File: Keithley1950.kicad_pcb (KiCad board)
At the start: 2 copper layers, 0 parts

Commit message: Initial placement on pcb
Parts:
- added C1: 47uF, Capacitor_SMD:CP_Elec_6.3x5.9, F.Cu at (78.0, 52.0)
- added C10: 1uF, Capacitor_SMD:C_0805_2012Metric, F.Cu at (60.2, 98.5)
- added C11: .1uF, Capacitor_SMD:C_0603_1608Metric, B.Cu at (72.8, 58.8)
- added C12: 3.3uF, Capacitor_SMD:C_0603_1608Metric, F.Cu at (66.8, 103.0)
- added C13: .1uF, Capacitor_SMD:C_0603_1608Metric, F.Cu at (70.2, 103.0)
- added C14: .1uF, Capacitor_SMD:C_0603_1608Metric, F.Cu at (40.8, 51.2)
- added C15: .1uF, Capacitor_SMD:C_0603_1608Metric, B.Cu at (53.6, 44.8)
- added C16: .1uF, Capacitor_SMD:C_0603_1608Metric, F.Cu at (67.8, 77.8)
- added C17: .1uF, Capacitor_SMD:C_0603_1608Metric, B.Cu at (59.2, 37.2)
- added C18: .1uF, Capacitor_SMD:C_0603_1608Metric, F.Cu at (60.2, 74.2)
- added C19: 610pF, Capacitor_SMD:C_0805_2012Metric, F.Cu at (55.0, 64.2)
- added C2: 47uF, Capacitor_SMD:CP_Elec_6.3x5.9, F.Cu at (69.5, 52.0)
- added C20: 110pF, Capacitor_SMD:C_0805_2012Metric, F.Cu at (55.0, 73.2)
- added C21: 5pF, project:MURATA_TZ03, F.Cu at (68.5, 84.0)
- added C22: 47pF, Capacitor_SMD:C_0805_2012Metric, F.Cu at (64.5, 63.5)
- added C23: 0.1uF, Capacitor_THT:C_Rect_L18.0mm_W5.0mm_P15.00mm_FKS3_FKP3, F.Cu at (55.5, 92.0)
- added C24: 5pF, project:MURATA_TZ03, F.Cu at (57.0, 84.0)
- added C3: 47uF, Capacitor_SMD:CP_Elec_6.3x5.9, F.Cu at (61.0, 52.0)
- added C4: 470pF, Capacitor_SMD:C_0805_2012Metric, F.Cu at (83.0, 54.8)
- added C5: .1uF, Capacitor_SMD:C_0603_1608Metric, B.Cu at (69.5, 55.0)
- added C6: .1uF, Capacitor_SMD:C_0603_1608Metric, F.Cu at (74.5, 101.2)
- added C7: 10uF, Capacitor_SMD:CP_Elec_5x5.4, F.Cu at (75.8, 95.5)
- added C8: .1uF, Capacitor_SMD:C_0603_1608Metric, F.Cu at (69.2, 90.5)
- added C9: 10uF, Capacitor_SMD:C_0805_2012Metric, F.Cu at (62.8, 95.5)
- added D1: S3M, Diode_SMD:D_SMB-SMC_Universal_Handsoldering, B.Cu at (61.5, 32.0)
- added D2: S3M, Diode_SMD:D_SMB-SMC_Universal_Handsoldering, B.Cu at (73.5, 32.0)
- added D3: S3M, Diode_SMD:D_SMB-SMC_Universal_Handsoldering, B.Cu at (67.5, 39.0)
- added D4: S3M, Diode_SMD:D_SMB-SMC_Universal_Handsoldering, B.Cu at (61.5, 46.0)
- added D5: S3M, Diode_SMD:D_SMB-SMC_Universal_Handsoldering, B.Cu at (73.5, 46.0)
- added D6: S3M, Diode_SMD:D_SMB-SMC_Universal_Handsoldering, B.Cu at (63.0, 76.8)
- added D7: S3M, Diode_SMD:D_SMB-SMC_Universal_Handsoldering, B.Cu at (63.0, 69.8)
- added H1: MountingHole_Pad, MountingHole:MountingHole_3.2mm_M3_Pad_Via, F.Cu at (85.0, 105.0)
- added H2: MountingHole_Pad, MountingHole:MountingHole_3.2mm_M3_Pad_Via, F.Cu at (34.2, 58.5)
- added H3: MountingHole_Pad, MountingHole:MountingHole_3.2mm_M3_Pad_Via, F.Cu at (85.0, 25.0)
- added J1: Conn_01x14, Package_DIP:DIP-14_W7.62mm_Socket_LongPads, F.Cu at (80.0, 59.0)
- added J2: Conn_01x03, TerminalBlock_Phoenix:TerminalBlock_Phoenix_PT-1,5-3-5.0-H_1x03_P5.00mm_Horizontal, F.Cu at (84.0, 37.0)
- added J3: Conn_01x02, TerminalBlock_Phoenix:TerminalBlock_Phoenix_PT-1,5-2-5.0-H_1x02_P5.00mm_Horizontal, F.Cu at (84.0, 96.0)
- added K1: Relay_SP2P, Relay_THT:Relay_SPST_StandexMeder_SIL_Form1A, F.Cu at (48.2, 47.5)
- added K2: Relay_SP2P, Relay_THT:Relay_SPST_StandexMeder_SIL_Form1A, F.Cu at (48.2, 40.8)
- added K3: Relay_SP3P, Relay_THT:Relay_SPDT_SANYOU_SRD_Series_Form_C, F.Cu at (32.2, 28.8)
- added K4: Relay_SP2P, Relay_THT:Relay_SPST_StandexMeder_SIL_Form1A, F.Cu at (48.2, 65.5)
- added K5: Relay_SP2P, Relay_THT:Relay_SPST_StandexMeder_SIL_Form1A, F.Cu at (48.2, 72.2)
- added K6: Relay_SP3P, Relay_THT:Relay_SPDT_SANYOU_SRD_Series_Form_C, F.Cu at (32.2, 101.2)
- added K7: Relay_SP3P, Relay_THT:Relay_SPDT_SANYOU_SRD_Series_Form_C, F.Cu at (32.2, 84.2)
- added Q1: MMBFJ111, Package_TO_SOT_SMD:SOT-23, F.Cu at (54.5, 44.5)
- added Q2: MMBFJ111, Package_TO_SOT_SMD:SOT-23, F.Cu at (84.8, 50.8)
- added Q3: MMBFJ111, Package_TO_SOT_SMD:SOT-23, F.Cu at (54.5, 40.0)
- added Q4: MMBFJ111, Package_TO_SOT_SMD:SOT-23, F.Cu at (86.5, 78.0)
- added Q5: MMBT3906, Package_TO_SOT_SMD:SOT-23, F.Cu at (49.0, 59.0)
- added Q6: MMBT3906, Package_TO_SOT_SMD:SOT-23, F.Cu at (49.0, 55.0)
- added Q7: MMBFJ111, Package_TO_SOT_SMD:SOT-23, F.Cu at (64.5, 60.0)
- added Q8: MMBT3906, Package_TO_SOT_SMD:SOT-23, F.Cu at (68.5, 60.0)
- added R1: 10k, Resistor_SMD:R_0805_2012Metric, B.Cu at (76.0, 38.5)
- added R10: 4R7, Resistor_SMD:R_0805_2012Metric, F.Cu at (59.0, 36.5)
- added R11: 100k, Resistor_SMD:R_0805_2012Metric, F.Cu at (82.5, 78.0)
- added R12: 4R3, Resistor_SMD:R_0805_2012Metric, F.Cu at (63.5, 36.5)
- added R13: 5R1, Resistor_SMD:R_2512_6332Metric, B.Cu at (85.0, 52.5)
- added R14: R47, Resistor_SMD:R_2512_6332Metric, F.Cu at (66.5, 31.5)
- added R15: R43, Resistor_SMD:R_2512_6332Metric, F.Cu at (57.5, 31.5)
- added R16: 10k, Resistor_SMD:R_0805_2012Metric, F.Cu at (54.0, 59.8)
- added R17: 0R1, project:R_2512_With_10mm_axial, F.Cu at (62.0, 25.0)
- added R18: 10k, Resistor_SMD:R_0805_2012Metric, F.Cu at (54.0, 55.8)
- added R19: 10M, Resistor_SMD:R_0805_2012Metric, F.Cu at (62.8, 99.0)
- added R2: 10k, Resistor_SMD:R_0805_2012Metric, B.Cu at (78.5, 38.5)
- added R20: 2k, Resistor_SMD:R_0805_2012Metric, F.Cu at (55.0, 66.8)
- added R21: 27k, Resistor_SMD:R_0805_2012Metric, F.Cu at (66.0, 69.0)
- added R22: 10k, Resistor_SMD:R_0805_2012Metric, F.Cu at (55.0, 70.8)
- added R23: 24k, Resistor_SMD:R_0805_2012Metric, F.Cu at (64.5, 66.0)
- added R24: 3k, Resistor_SMD:R_0805_2012Metric, F.Cu at (62.0, 69.0)
- added R25: 1M, Resistor_SMD:R_0805_2012Metric, F.Cu at (62.5, 85.0)
- added R26: 1M, Resistor_SMD:R_0805_2012Metric, F.Cu at (58.0, 78.0)
- added R27: 10k, Resistor_SMD:R_0805_2012Metric, F.Cu at (87.0, 86.5)
- added R28: 100k, Resistor_SMD:R_0805_2012Metric, F.Cu at (68.5, 63.5)
- added R3: 470R, Resistor_SMD:R_0805_2012Metric, F.Cu at (59.0, 43.5)
- added R4: 100k, Resistor_SMD:R_0805_2012Metric, B.Cu at (51.5, 41.5)
- added R5: 430R, Resistor_SMD:R_0805_2012Metric, F.Cu at (63.5, 43.5)
- added R6: 47R, Resistor_SMD:R_0805_2012Metric, F.Cu at (63.5, 40.0)
- added R7: 100k, Resistor_SMD:R_0805_2012Metric, F.Cu at (85.8, 54.8)
- added R8: 100k, Resistor_SMD:R_0805_2012Metric, B.Cu at (51.5, 37.0)
- added R9: 43R, Resistor_SMD:R_0805_2012Metric, F.Cu at (59.0, 40.0)
- added TP1: TestPoint, TestPoint:TestPoint_Pad_D2.5mm, F.Cu at (58.2, 46.2)
- added TP2: TestPoint, TestPoint:TestPoint_Pad_D2.5mm, F.Cu at (82.5, 82.5)
- added TP3: TestPoint, TestPoint:TestPoint_Pad_D2.5mm, F.Cu at (63.0, 91.0)
- added TP4: TestPoint, TestPoint:TestPoint_Pad_D2.5mm, F.Cu at (61.0, 105.0)
- added TP5: TestPoint, TestPoint:TestPoint_Pad_D2.5mm, F.Cu at (69.5, 73.5)
- added U1: TL082, Package_SO:SOIC-8_3.9x4.9mm_P1.27mm, B.Cu at (55.5, 39.0)
- added U2: LM339, Package_SO:SOIC-14_3.9x8.7mm_P1.27mm, F.Cu at (71.2, 41.0)
- added U3: 74LS138, Package_SO:SOIC-16_3.9x9.9mm_P1.27mm, B.Cu at (63.0, 58.0)
- added U4: AD8436, Package_SO:QSOP-20_3.9x8.7mm_P0.635mm, F.Cu at (68.2, 97.0)
- added U5: ULN2003, Package_SO:SOIC-16_3.9x9.9mm_P1.27mm, F.Cu at (42.5, 57.2)
- added U6: 74HC4094, Package_SO:SOIC-16_3.9x9.9mm_P1.27mm, B.Cu at (74.5, 65.0)
- added U7: TL082, Package_SO:SOIC-8_3.9x4.9mm_P1.27mm, F.Cu at (64.0, 76.0)
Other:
- board outline added: 60 x 90 mm
- net class Default: trace_width 0.25 -> 0.3
- net class pwr added: clearance 0.3, trace_width 0.5, via_dia 1, via_drill 0.6
- rule pad_to_mask_clearance: 0.051 -> 0.02
- rule solder_mask_min_width: 0.25 -> 0.19
- rule trace_min: 0.2 -> 0.3

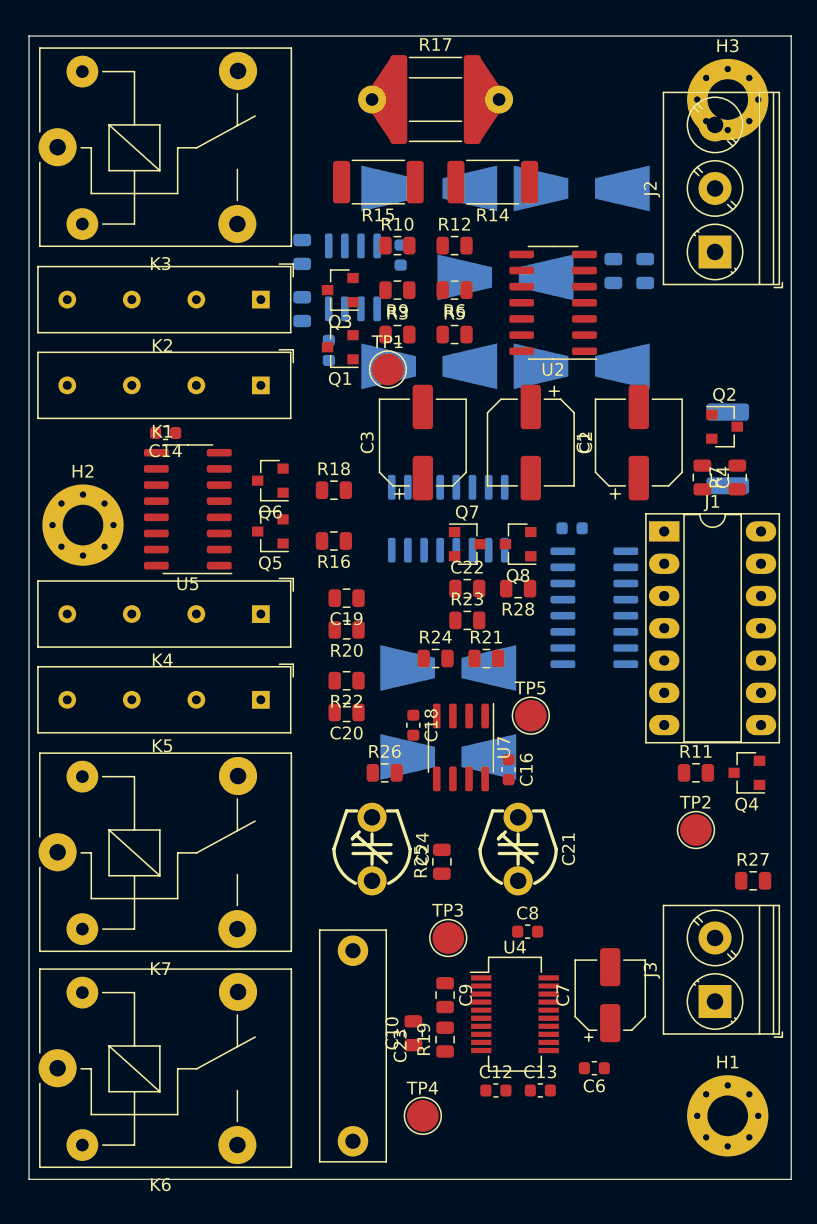
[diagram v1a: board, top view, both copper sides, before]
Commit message: Optimized placement
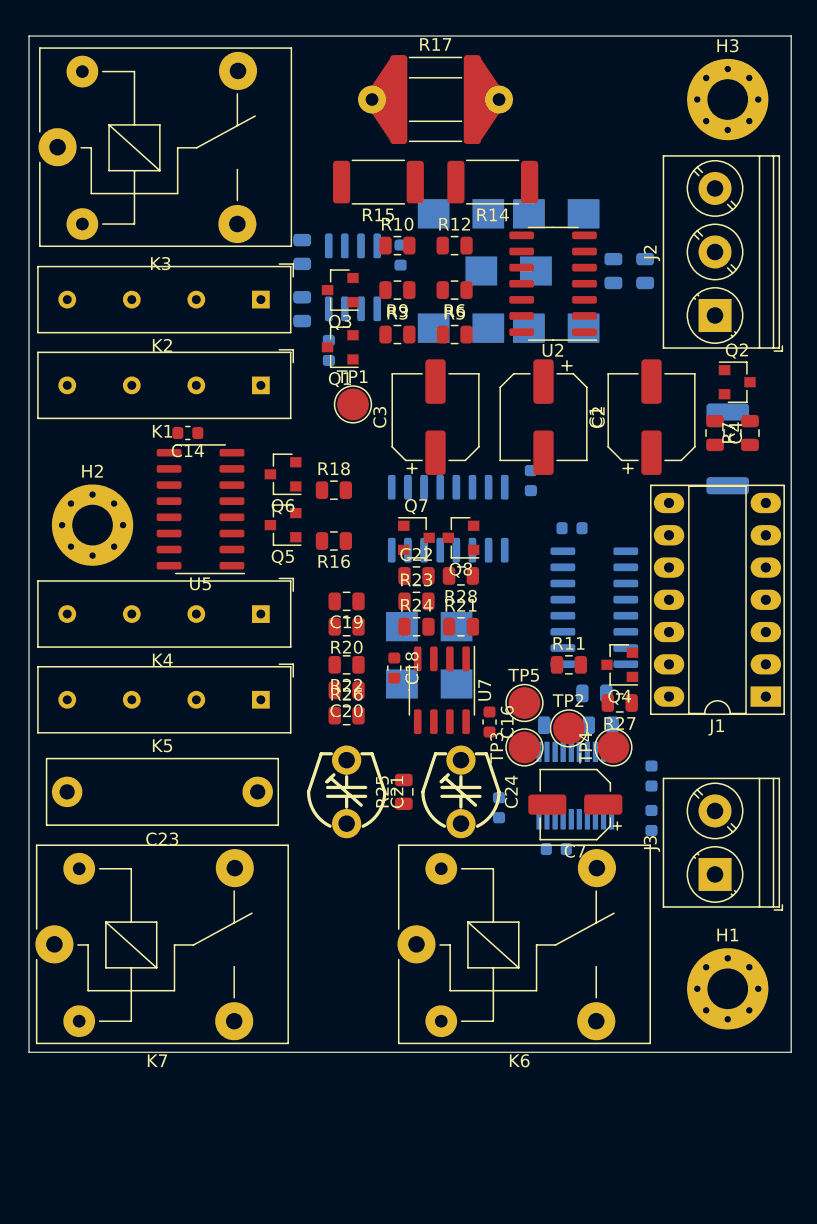
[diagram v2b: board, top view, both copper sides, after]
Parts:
- C10, C12, C13, C6, C8, C9, R19, U4: moved to B.Cu
- D1, D2, D3, D4, D5, D6, D7: footprint Diode_SMD:D_SMB-SMC_Universal_Handsoldering -> Diode_SMD:D_SMB
- moved TP4 32.6 mm to (76.0, 76.0), turned to 90 degrees
- moved C10 30.3 mm to (74.5, 71.8), turned to 180 degrees
- moved K6 29.9 mm to (60.5, 91.5)
- moved C12 27.6 mm to (79.0, 78.2), turned to 270 degrees
- moved R19 27.6 mm to (75.0, 74.2), turned to 180 degrees
- moved C13 23.0 mm to (79.0, 81.8), turned to 270 degrees
- moved C9 23.0 mm to (71.5, 74.2), turned to 0 degrees
- moved U4 18.6 mm to (73.0, 79.0), turned to 270 degrees
- moved C6 17.5 mm to (71.5, 84.0), turned to 0 degrees
- moved R27 17.5 mm to (76.5, 72.5), turned to 180 degrees
- moved TP3 16.2 mm to (69.0, 76.0), turned to 90 degrees
- moved J1 15.3 mm to (88.0, 72.0), turned to 180 degrees
- moved C7 15.2 mm to (73.0, 80.5), turned to 180 degrees
- moved C23 14.6 mm to (48.0, 79.5), turned to 180 degrees
- moved C21 14.2 mm to (55.0, 79.5)
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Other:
- board size 60 x 90 mm -> 60 x 80 mm

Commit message: More optimizations
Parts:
- C12: footprint Capacitor_SMD:C_0603_1608Metric -> Capacitor_SMD:C_0805_2012Metric
- R1, R2: moved to F.Cu
- moved C6 4.74 mm to (67.0, 82.5), turned to 270 degrees
- moved R2 3.30 mm to (77.0, 35.6), turned to 90 degrees
- moved D1 2.69 mm to (66.5, 33.0)
- moved D2 2.69 mm to (74.0, 33.0)
- moved D3 2.69 mm to (70.2, 37.5)
- moved D4 2.69 mm to (66.5, 42.0)
- moved D5 2.69 mm to (74.0, 42.0)
- moved C15 2.12 mm to (55.1, 46.2)
- moved C17 2.12 mm to (60.8, 38.8)
- moved R4 2.12 mm to (53.0, 43.0)
- moved R8 2.12 mm to (53.0, 38.5)
- moved U1 2.12 mm to (57.0, 40.5)
- moved R13 1.80 mm to (84.0, 51.0), turned to 180 degrees
- moved C8 1.75 mm to (67.0, 79.0)
- moved R1 1.41 mm to (77.0, 39.5)

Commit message: Manual routing done
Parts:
- R27: moved to B.Cu
- moved R27 14.2 mm to (74.0, 58.5)
- moved R16 6.54 mm to (54.8, 53.2)
- moved R28 6.50 mm to (64.0, 56.0), turned to 0 degrees
- moved Q5 5.80 mm to (50.8, 52.8)
- moved C11 2.50 mm to (70.2, 58.8)
- moved Q6 2.14 mm to (50.8, 56.5)
- moved C23 1.00 mm to (49.0, 79.5)
- moved H2 1.00 mm to (36.0, 58.5)
- moved K1 1.00 mm to (49.2, 47.5)
- moved K2 1.00 mm to (49.2, 40.8)
- moved K3 1.00 mm to (33.2, 28.8)
- moved K4 1.00 mm to (49.2, 65.5)
- moved K5 1.00 mm to (49.2, 72.2)
- moved K7 1.00 mm to (33.0, 91.5)
- moved R18 0.79 mm to (54.8, 55.5)
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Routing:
- net GNDA: track 0.00 -> 254.4 mm, vias 0 -> 19
- net +5V: track 0.00 -> 195.4 mm, vias 0 -> 2
- net -15V: track 0.00 -> 119.7 mm, vias 0 -> 2
- net /AMPS_INP: track 0.00 -> 112.5 mm
- net +15V: track 0.00 -> 106.4 mm, vias 0 -> 6
- net /SHUNT_SIGNAL: track 0.00 -> 98.4 mm, vias 0 -> 6
- net /INPUT_LO: track 0.00 -> 84.2 mm
- net Net-(C21-Pad2): track 0.00 -> 58.4 mm, vias 0 -> 1
- net Net-(K6-Pad5): track 0.00 -> 49.7 mm, vias 0 -> 1
- net Net-(K3-Pad5): track 0.00 -> 42.1 mm
- net /SHUNT_TRMS_SW: track 0.00 -> 41.7 mm, vias 0 -> 1
- net Net-(U3-Pad5): track 0.00 -> 39.3 mm, vias 0 -> 3
- net Net-(U5-Pad4): track 0.00 -> 34.8 mm, vias 0 -> 3
- net /SIGNAL_GUARD: track 0.00 -> 34.4 mm, vias 0 -> 1
- net Net-(U5-Pad3): track 0.00 -> 33.1 mm, vias 0 -> 3
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- added copper zone on B.Cu, net GNDA
- added copper zone on F.Cu, net GNDA
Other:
- net class pwr: clearance 0.3 -> 0.2

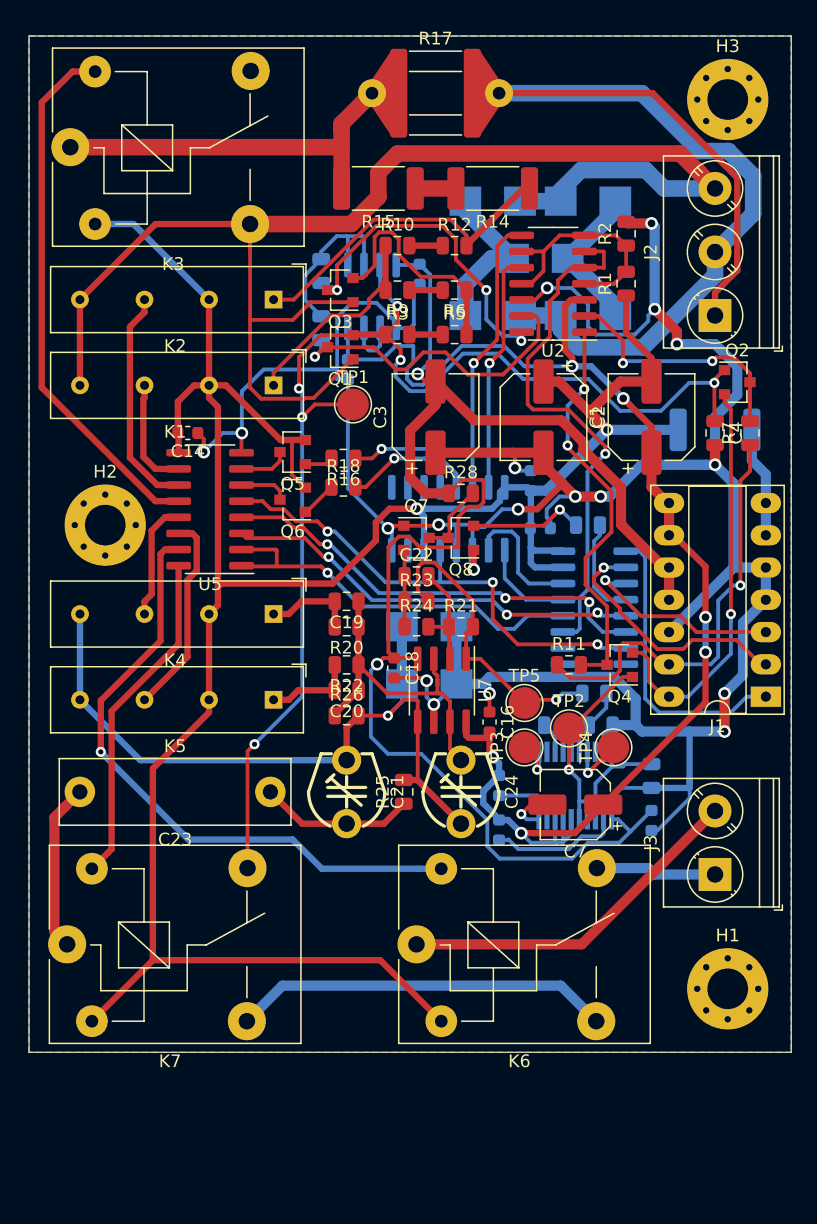
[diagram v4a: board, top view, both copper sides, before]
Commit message: Clean up silkscreen, add logos
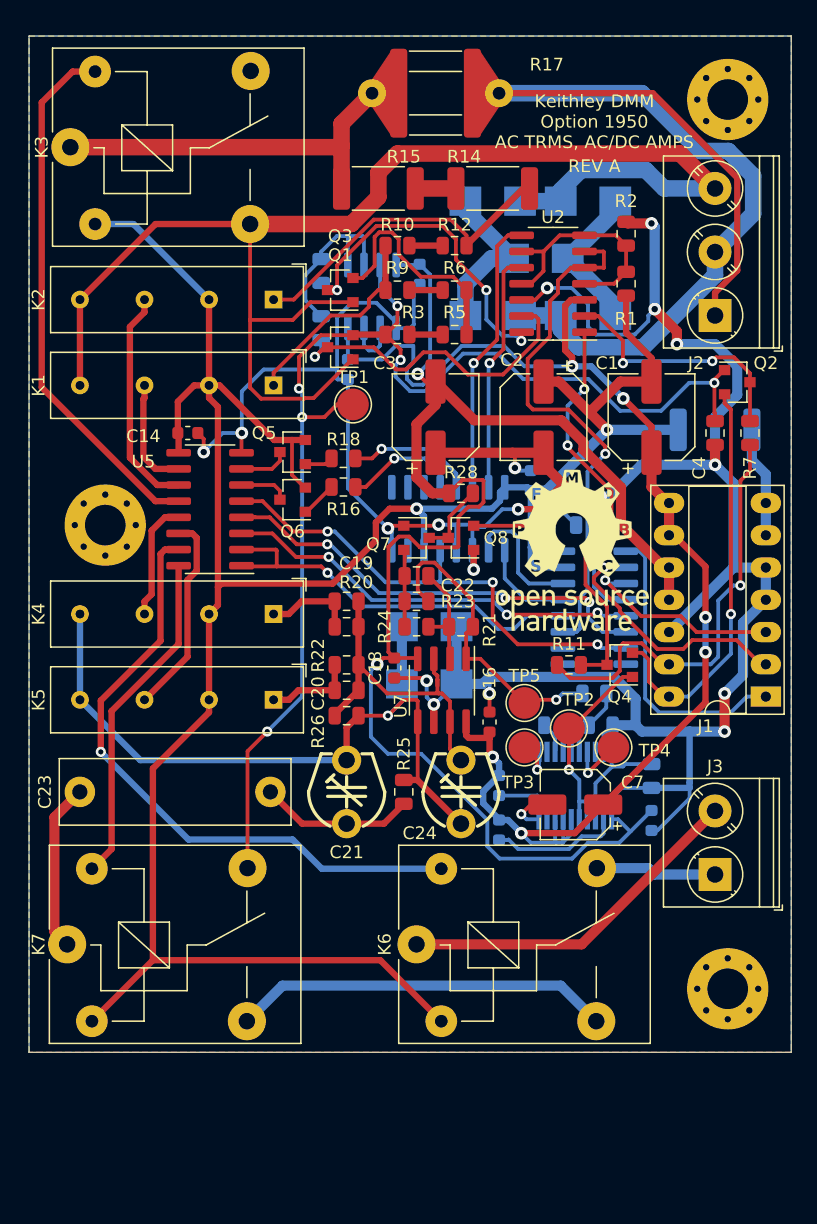
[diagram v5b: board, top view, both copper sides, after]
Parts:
- added LOGO***: OSHW_LOGO, project:oshw-logo, F.Cu at (72.8, 60.5)
- added LOGO***: LOGO, project:osp-logo, B.Cu at (71.5, 91.5)
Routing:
- net -15V: track 119.7 -> 119.0 mm
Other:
- net class pwr: via_drill 0.6 -> 0.5
- board text added: "Keithley DMM Option 1950 AC TRMS, AC/DC AMPS"
- board text added: "REV A"
